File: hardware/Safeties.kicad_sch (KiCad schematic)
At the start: 11 parts, among them Q1 2N7002, Q2 2N7002, U14 74AUP1G32

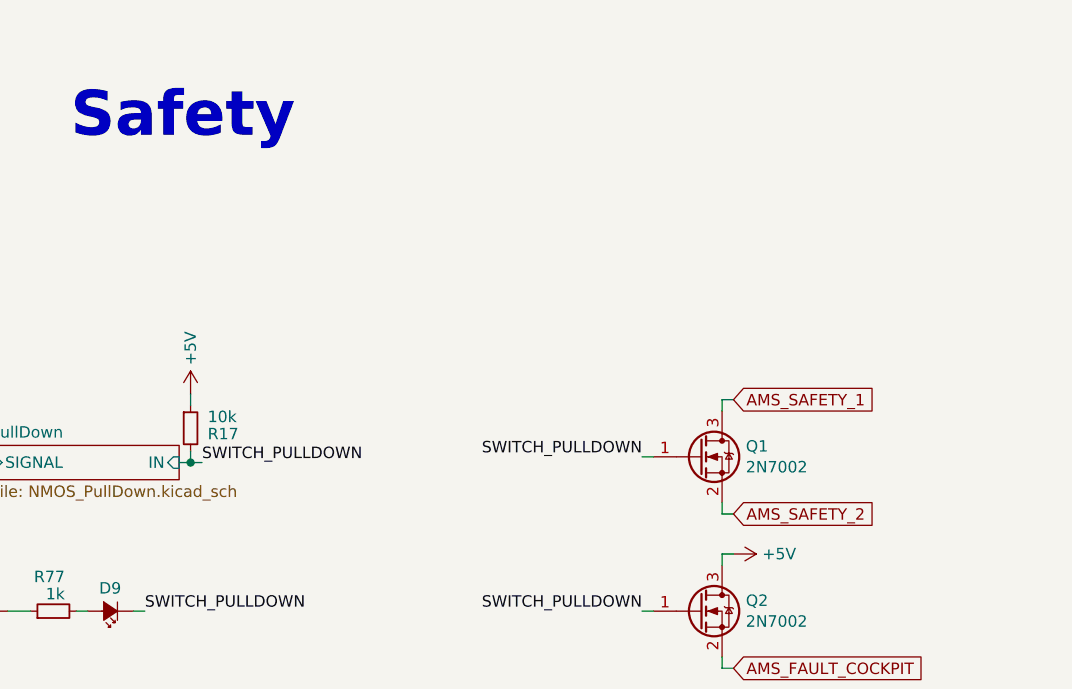
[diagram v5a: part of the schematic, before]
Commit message: changed HV measurements from isolated opamp to isolated ADC with isolated spi communication, changed safety laatching from mosfet back to relay
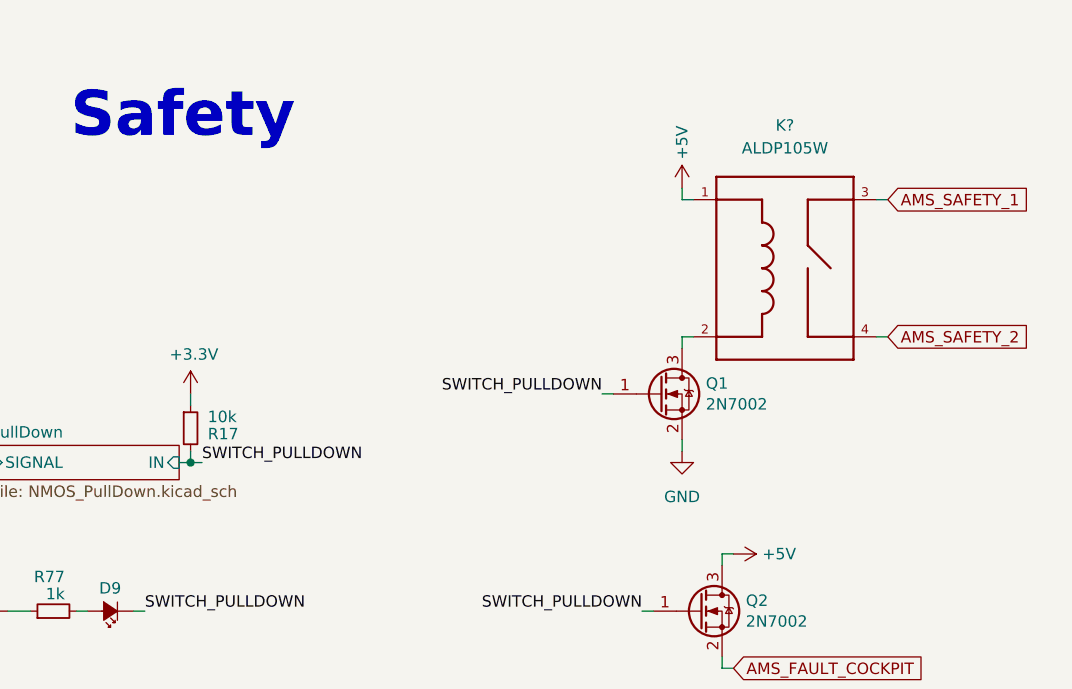
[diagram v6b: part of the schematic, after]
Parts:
- added K?: ALDP105W, RELAY_ALDP105W, symbol PUTM_EV_BMS_library:ALDP105W
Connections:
- net +3V3: now also R17.1
- net +5V: now also K?.1; no longer R17.1
- net AMS_SAFETY_1: now also K?.3; no longer Q1.3 (D)
- net AMS_SAFETY_2: now also K?.4; no longer Q1.2 (S)
- net GND: now also Q1.2 (S)
- new net: K?.2, Q1.3 (D)
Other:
- moved on the sheet: Q1
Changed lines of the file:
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@@
     (stroke (width 0) (type default) (color 0 0 0 0))
   )
-  (wire (pts (xy 213.36 60.325) (xy 214.63 60.325))
+  (wire (pts (xy 208.915 53.34) (xy 210.185 53.34))
     (stroke (width 0) (type default) (color 0 0 0 0))
   )
@@
   )
   (wire (pts (xy 142.24 126.365) (xy 142.24 128.27))
+    (stroke (width 0) (type default) (color 0 0 0 0))
+  )
+  (wire (pts (xy 219.075 31.75) (xy 217.805 31.75))
     (stroke (width 0) (type default) (color 0 0 0 0))
   )
@@
     (stroke (width 0) (type default) (color 0 0 0 0))
   )
+  (wire (pts (xy 217.805 46.99) (xy 219.075 46.99))
+    (stroke (width 0) (type default) (color 0 0 0 0))
+  )
   (polyline (pts (xy 162.56 138.43) (xy 162.56 134.62))
     (stroke (width 0) (type default) (color 0 0 0 0))
@@
     (stroke (width 0) (type default) (color 0 0 0 0))
   )
-  (wire (pts (xy 223.52 66.675) (xy 222.25 66.675))
+  (wire (pts (xy 240.665 46.99) (xy 239.395 46.99))
     (stroke (width 0) (type default) (color 0 0 0 0))
   )
@@
     (stroke (width 0) (type default) (color 0 0 0 0))
   )
+  (wire (pts (xy 217.805 30.48) (xy 217.805 31.75))
+    (stroke (width 0) (type default) (color 0 0 0 0))
+  )
   (wire (pts (xy 142.24 134.62) (xy 142.24 135.89))
     (stroke (width 0) (type default) (color 0 0 0 0))
@@
     (stroke (width 0) (type default) (color 0 0 0 0))
   )
-  (wire (pts (xy 222.25 53.975) (xy 222.25 55.245))
+  (wire (pts (xy 217.805 46.99) (xy 217.805 48.26))
     (stroke (width 0) (type default) (color 0 0 0 0))
   )
@@
     (stroke (width 0) (type default) (color 0 0 0 0))
   )
-  (wire (pts (xy 222.25 65.405) (xy 222.25 66.675))
+  (wire (pts (xy 217.805 58.42) (xy 217.805 59.69))
     (stroke (width 0) (type default) (color 0 0 0 0))
   )
@@
     (stroke (width 0) (type default) (color 0 0 0 0))
   )
-  (wire (pts (xy 223.52 53.975) (xy 222.25 53.975))
+  (wire (pts (xy 240.665 31.75) (xy 239.395 31.75))
     (stroke (width 0) (type default) (color 0 0 0 0))
   )
@@
     (effects (font (size 1.27 1.27)) (justify left bottom))
   )
-  (label "SWITCH_PULLDOWN" (at 213.36 60.325 180)
+  (label "SWITCH_PULLDOWN" (at 208.915 53.34 180)
     (effects (font (size 1.27 1.27)) (justify right bottom))
   )
@@
     )
   )
-  (global_label "AMS_SAFETY_2" (shape input) (at 223.52 66.675 0) (fields_autoplaced)
-    (effects (font (size 1.27 1.27)) (justify left))
-    (property "Intersheet References" "${INTERSHEET_REFS}" (id 0) (at 239.3304 66.5956 0)
+  (global_label "AMS_SAFETY_2" (shape input) (at 240.665 46.99 0) (fields_autoplaced)
+    (effects (font (size 1.27 1.27)) (justify left))
+    (property "Intersheet References" "${INTERSHEET_REFS}" (id 0) (at 256.4754 46.9106 0)
       (effects (font (size 1.27 1.27)) (justify left) hide)
     )
@@
     )
   )
-  (global_label "AMS_SAFETY_1" (shape input) (at 223.52 53.975 0) (fields_autoplaced)
-    (effects (font (size 1.27 1.27)) (justify left))
-    (property "Intersheet References" "${INTERSHEET_REFS}" (id 0) (at 239.3304 54.0544 0)
+  (global_label "AMS_SAFETY_1" (shape input) (at 240.665 31.75 0) (fields_autoplaced)
+    (effects (font (size 1.27 1.27)) (justify left))
+    (property "Intersheet References" "${INTERSHEET_REFS}" (id 0) (at 256.4754 31.8294 0)
       (effects (font (size 1.27 1.27)) (justify left) hide)
     )
@@
     (effects (font (size 1.27 1.27)) (justify left))
   )
+  (symbol (lib_id "power:GND") (at 217.805 59.69 0) (unit 1)
+    (in_bom yes) (on_board yes) (fields_autoplaced)
+    (property "Reference" "#PWR?" (id 0) (at 217.805 66.04 0)
+      (effects (font (size 1.27 1.27)) hide)
+    )
+    (property "Value" "GND" (id 1) (at 217.805 64.77 0))
+    (property "Footprint" "" (id 2) (at 217.805 59.69 0)
+      (effects (font (size 1.27 1.27)) hide)
+    )
+    (property "Datasheet" "" (id 3) (at 217.805 59.69 0)
+      (effects (font (size 1.27 1.27)) hide)
+    )
+    (pin "1")
+  )
   (symbol (lib_id "Transistor_FET:2N7002") (at 219.71 77.47 0) (unit 1)
     (in_bom yes) (on_board yes)
@@
     (pin "1")
   )
+  (symbol (lib_id "power:+3.3V") (at 163.195 53.34 0) (unit 1)
+    (in_bom yes) (on_board yes)
+    (property "Reference" "#PWR?" (id 0) (at 163.195 57.15 0)
+      (effects (font (size 1.27 1.27)) hide)
+    )
+    (property "Value" "+3.3V" (id 1) (at 163.576 48.9458 0))
+    (property "Footprint" "" (id 2) (at 163.195 53.34 0)
+      (effects (font (size 1.27 1.27)) hide)
+    )
+    (property "Datasheet" "" (id 3) (at 163.195 53.34 0)
+      (effects (font (size 1.27 1.27)) hide)
+    )
+    (pin "1")
+  )
   (symbol (lib_id "Device:R_Small") (at 163.195 57.15 0) (unit 1)
     (in_bom yes) (on_board yes)
@@
     (pin "2")
   )
+  (symbol (lib_id "PUTM_EV_BMS_library:ALDP105W") (at 229.235 39.37 0) (unit 1)
+    (in_bom yes) (on_board yes) (fields_autoplaced)
+    (property "Reference" "K?" (id 0) (at 229.235 23.495 0))
+    (property "Value" "ALDP105W" (id 1) (at 229.235 26.035 0))
+    (property "Footprint" "RELAY_ALDP105W" (id 2) (at 229.235 39.37 0)
+      (effects (font (size 1.27 1.27)) (justify left bottom) hide)
+    )
+    (property "Datasheet" "" (id 3) (at 229.235 39.37 0)
+      (effects (font (size 1.27 1.27)) (justify left bottom) hide)
+    )
+    (property "STANDART" "Manufacturer Recommendations" (id 4) (at 229.235 39.37 0)
+      (effects (font (size 1.27 1.27)) (justify left bottom) hide)
+    )
+    (property "MF" "Panasonic" (id 5) (at 229.235 39.37 0)
+      (effects (font (size 1.27 1.27)) (justify left bottom) hide)
+    )
+    (property "PARTREV" "N/A" (id 6) (at 229.235 39.37 0)
+      (effects (font (size 1.27 1.27)) (justify left bottom) hide)
+    )
+    (pin "1")
+    (pin "2")
+    (pin "3")
+    (pin "4")
+  )
   (symbol (lib_id "Device:R_Small") (at 147.955 77.47 90) (unit 1)
     (in_bom yes) (on_board yes)
@@
     )
     (property "Datasheet" "" (id 3) (at 142.24 120.015 0)
-      (effects (font (size 1.27 1.27)) hide)
-    )
-    (pin "1")
-  )
-  (symbol (lib_id "power:+5V") (at 163.195 53.34 0) (unit 1)
-    (in_bom yes) (on_board yes)
-    (property "Reference" "#PWR0118" (id 0) (at 163.195 57.15 0)
-      (effects (font (size 1.27 1.27)) hide)
-    )
-    (property "Value" "+5V" (id 1) (at 163.195 48.26 90))
-    (property "Footprint" "" (id 2) (at 163.195 53.34 0)
-      (effects (font (size 1.27 1.27)) hide)
-    )
-    (property "Datasheet" "" (id 3) (at 163.195 53.34 0)
       (effects (font (size 1.27 1.27)) hide)
     )
@@
     (pin "2")
   )
-  (symbol (lib_id "Transistor_FET:2N7002") (at 219.71 60.325 0) (unit 1)
-    (in_bom yes) (on_board yes)
-    (property "Reference" "Q1" (id 0) (at 224.8916 59.1566 0)
-      (effects (font (size 1.27 1.27)) (justify left))
-    )
-    (property "Value" "2N7002" (id 1) (at 224.8916 61.468 0)
-      (effects (font (size 1.27 1.27)) (justify left))
-    )
-    (property "Footprint" "Package_TO_SOT_SMD:SOT-23" (id 2) (at 224.79 62.23 0)
+  (symbol (lib_id "Transistor_FET:2N7002") (at 215.265 53.34 0) (unit 1)
+    (in_bom yes) (on_board yes)
+    (property "Reference" "Q1" (id 0) (at 220.4466 52.1716 0)
+      (effects (font (size 1.27 1.27)) (justify left))
+    )
+    (property "Value" "2N7002" (id 1) (at 220.4466 54.483 0)
+      (effects (font (size 1.27 1.27)) (justify left))
+    )
+    (property "Footprint" "Package_TO_SOT_SMD:SOT-23" (id 2) (at 220.345 55.245 0)
       (effects (font (size 1.27 1.27) italic) (justify left) hide)
     )
-    (property "Datasheet" "https://www.onsemi.com/pub/Collateral/NDS7002A-D.PDF" (id 3) (at 219.71 60.325 0)
+    (property "Datasheet" "https://www.onsemi.com/pub/Collateral/NDS7002A-D.PDF" (id 3) (at 215.265 53.34 0)
       (effects (font (size 1.27 1.27)) (justify left) hide)
     )
@@
     (pin "5")
   )
+  (symbol (lib_id "power:+5V") (at 217.805 30.48 0) (unit 1)
+    (in_bom yes) (on_board yes)
+    (property "Reference" "#PWR?" (id 0) (at 217.805 34.29 0)
+      (effects (font (size 1.27 1.27)) hide)
+    )
+    (property "Value" "+5V" (id 1) (at 217.805 25.4 90))
+    (property "Footprint" "" (id 2) (at 217.805 30.48 0)
+      (effects (font (size 1.27 1.27)) hide)
+    )
+    (property "Datasheet" "" (id 3) (at 217.805 30.48 0)
+      (effects (font (size 1.27 1.27)) hide)
+    )
+    (pin "1")
+  )
   (symbol (lib_id "Device:C_Small") (at 157.48 118.11 270) (unit 1)

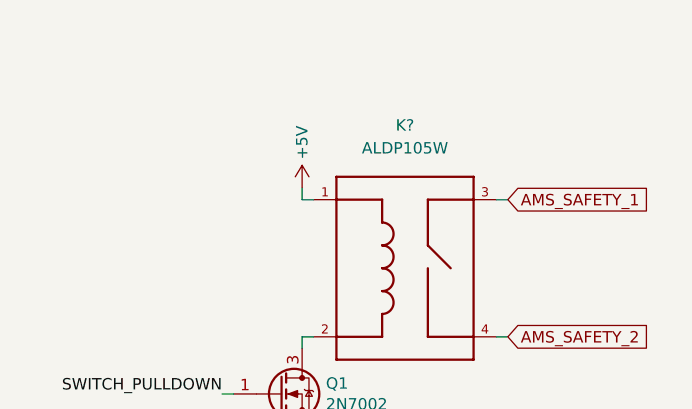
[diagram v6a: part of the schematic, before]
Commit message: changed the 1V voltage ref made from RL circuit to low noise, 0.1% error 1.024 V ref gen, and changed the opamp used for current sensor feedback filtration to a high precision low drift opamp
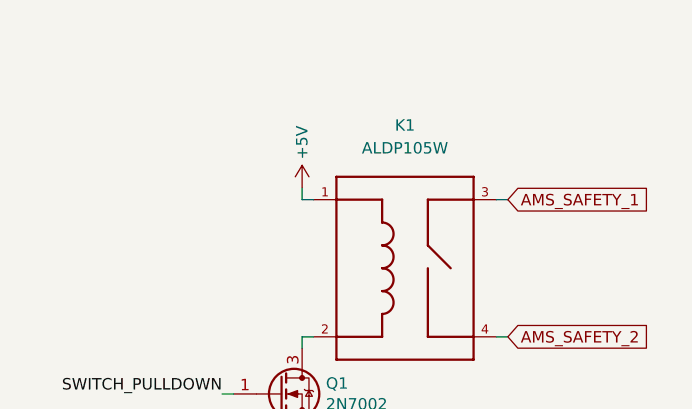
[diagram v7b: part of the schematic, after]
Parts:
- gave numbers to parts that had none: 1
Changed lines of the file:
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@@
   (symbol (lib_id "power:GND") (at 217.805 59.69 0) (unit 1)
     (in_bom yes) (on_board yes) (fields_autoplaced)
-    (property "Reference" "#PWR?" (id 0) (at 217.805 66.04 0)
+    (property "Reference" "#PWR0166" (id 0) (at 217.805 66.04 0)
       (effects (font (size 1.27 1.27)) hide)
     )
@@
   (symbol (lib_id "power:+3.3V") (at 163.195 53.34 0) (unit 1)
     (in_bom yes) (on_board yes)
-    (property "Reference" "#PWR?" (id 0) (at 163.195 57.15 0)
+    (property "Reference" "#PWR0156" (id 0) (at 163.195 57.15 0)
       (effects (font (size 1.27 1.27)) hide)
     )
@@
   (symbol (lib_id "PUTM_EV_BMS_library:ALDP105W") (at 229.235 39.37 0) (unit 1)
     (in_bom yes) (on_board yes) (fields_autoplaced)
-    (property "Reference" "K?" (id 0) (at 229.235 23.495 0))
+    (property "Reference" "K1" (id 0) (at 229.235 23.495 0))
     (property "Value" "ALDP105W" (id 1) (at 229.235 26.035 0))
     (property "Footprint" "RELAY_ALDP105W" (id 2) (at 229.235 39.37 0)
@@
   (symbol (lib_id "power:+5V") (at 217.805 30.48 0) (unit 1)
     (in_bom yes) (on_board yes)
-    (property "Reference" "#PWR?" (id 0) (at 217.805 34.29 0)
-      (effects (font (size 1.27 1.27)) hide)
-    )
+    (property "Reference" "#PWR0164" (id 0) (at 217.805 34.29 0)
+      (effects (font (size 1.27 1.27)) hide)
+    )

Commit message: schemat sync
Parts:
- removed Q2: 2N7002, Package_TO_SOT_SMD:SOT-23, symbol Transistor_FET:2N7002
- added Q4: 2N7002, Package_TO_SOT_SMD:SOT-23, symbol Transistor_FET:2N7002
- added R59: 100, Resistor_SMD:R_0603_1608Metric, symbol Device:R_Small
- added R61: 10k, Resistor_SMD:R_0603_1608Metric, symbol Device:R_Small
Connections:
- net SWITCH_PULLDOWN is gone; now on net AMS_FAULT_COCKPIT: D9.1 (K), Q1.1 (G), R17.2
- net +3V3: no longer R17.1
- net +5V: now also R17.1
- net AMS_FAULT: now also R59.2
- net AMS_FAULT_COCKPIT: now also Q4.3 (D)
- net GND: now also Q4.2 (S), R61.2
- new net: Q4.1 (G), R59.1, R61.1
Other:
- sheet HP_PullDown renamed AIR_P
- sheet HP_PullDown1 renamed AIR_M
- sheet HP_PullDown2 renamed AIR_PRE
- removed sheet PullDown
- moved on the sheet: C25, C30, D9, R17, R51, R52, R77, R92, U14
